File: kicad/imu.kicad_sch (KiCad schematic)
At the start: 3 parts, among them U7 BMI160

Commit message: checking shunt footprints
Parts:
- C36: renamed from C33; footprint (none) -> Capacitor_SMD:C_0402_1005Metric
- C37: renamed from C34; footprint (none) -> Capacitor_SMD:C_0402_1005Metric
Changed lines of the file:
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@@
 		(dnp no)
 		(fields_autoplaced yes)
-		(property "Reference" "#PWR043"
+		(property "Reference" "#PWR066"
 			(at 137.16 119.38 0)
 			(effects
@@
 			(project ""
 				(path "/83aea3b7-5b9b-498e-8d41-e84fae2f87fa/314ef610-7e67-4168-90f4-c11d9335fa4f"
-					(reference "#PWR043")
+					(reference "#PWR066")
 					(unit 1)
 				)
@@
 		(dnp no)
 		(fields_autoplaced yes)
-		(property "Reference" "C33"
+		(property "Reference" "C36"
 			(at 161.29 96.5199 0)
 			(effects
@@
 			)
 		)
-		(property "Footprint" ""
+		(property "Footprint" "Capacitor_SMD:C_0402_1005Metric"
 			(at 158.4452 101.6 0)
 			(effects
@@
 			(project ""
 				(path "/83aea3b7-5b9b-498e-8d41-e84fae2f87fa/314ef610-7e67-4168-90f4-c11d9335fa4f"
-					(reference "C33")
+					(reference "C36")
 					(unit 1)
 				)
@@
 		(dnp no)
 		(fields_autoplaced yes)
-		(property "Reference" "C34"
+		(property "Reference" "C37"
 			(at 173.99 96.5199 0)
 			(effects
@@
 			)
 		)
-		(property "Footprint" ""
+		(property "Footprint" "Capacitor_SMD:C_0402_1005Metric"
 			(at 171.1452 101.6 0)
 			(effects
@@
 			(project "resc"
 				(path "/83aea3b7-5b9b-498e-8d41-e84fae2f87fa/314ef610-7e67-4168-90f4-c11d9335fa4f"
-					(reference "C34")
+					(reference "C37")
 					(unit 1)
 				)
@@
 		(dnp no)
 		(fields_autoplaced yes)
-		(property "Reference" "#PWR042"
+		(property "Reference" "#PWR065"
 			(at 138.43 82.55 0)
 			(effects
@@
 			(project ""
 				(path "/83aea3b7-5b9b-498e-8d41-e84fae2f87fa/314ef610-7e67-4168-90f4-c11d9335fa4f"
-					(reference "#PWR042")
-					(unit 1)
-				)
+					(reference "#PWR065")
+					(unit 1)
+				)

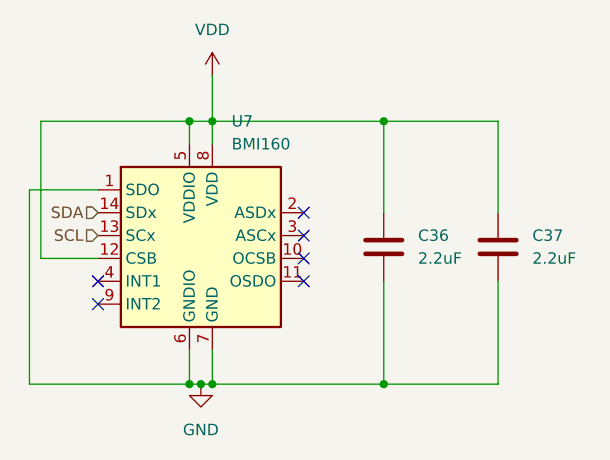
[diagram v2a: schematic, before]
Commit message: gate driver mostly schematic'd and pcb started
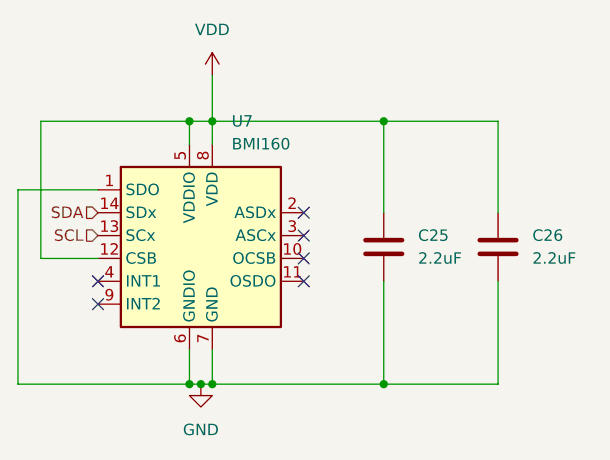
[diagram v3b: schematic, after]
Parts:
- renumbered C36 to C25, C37 to C26
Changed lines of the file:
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@@
 	(wire
 		(pts
-			(xy 118.11 113.03) (xy 135.89 113.03)
+			(xy 116.84 113.03) (xy 135.89 113.03)
 		)
 		(stroke
@@
 	(wire
 		(pts
-			(xy 125.73 91.44) (xy 118.11 91.44)
+			(xy 125.73 91.44) (xy 116.84 91.44)
 		)
 		(stroke
@@
 	(wire
 		(pts
-			(xy 118.11 91.44) (xy 118.11 113.03)
+			(xy 116.84 91.44) (xy 116.84 113.03)
 		)
 		(stroke
@@
 		(dnp no)
 		(fields_autoplaced yes)
-		(property "Reference" "#PWR066"
+		(property "Reference" "#PWR053"
 			(at 137.16 119.38 0)
 			(effects
@@
 			(project ""
 				(path "/83aea3b7-5b9b-498e-8d41-e84fae2f87fa/314ef610-7e67-4168-90f4-c11d9335fa4f"
-					(reference "#PWR066")
+					(reference "#PWR053")
 					(unit 1)
 				)
@@
 		(dnp no)
 		(fields_autoplaced yes)
-		(property "Reference" "C36"
+		(property "Reference" "C25"
 			(at 161.29 96.5199 0)
 			(effects
@@
 			(project ""
 				(path "/83aea3b7-5b9b-498e-8d41-e84fae2f87fa/314ef610-7e67-4168-90f4-c11d9335fa4f"
-					(reference "C36")
+					(reference "C25")
 					(unit 1)
 				)
@@
 		(dnp no)
 		(fields_autoplaced yes)
-		(property "Reference" "C37"
+		(property "Reference" "C26"
 			(at 173.99 96.5199 0)
 			(effects
@@
 			(project "resc"
 				(path "/83aea3b7-5b9b-498e-8d41-e84fae2f87fa/314ef610-7e67-4168-90f4-c11d9335fa4f"
-					(reference "C37")
+					(reference "C26")
 					(unit 1)
 				)
@@
 		(dnp no)
 		(fields_autoplaced yes)
-		(property "Reference" "#PWR065"
+		(property "Reference" "#PWR052"
 			(at 138.43 82.55 0)
 			(effects
@@
 			(project ""
 				(path "/83aea3b7-5b9b-498e-8d41-e84fae2f87fa/314ef610-7e67-4168-90f4-c11d9335fa4f"
-					(reference "#PWR065")
+					(reference "#PWR052")
 					(unit 1)
 				)

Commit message: rev3 ordered
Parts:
- renumbered C25 to C36, C26 to C37
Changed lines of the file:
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@@
 		(dnp no)
 		(fields_autoplaced yes)
-		(property "Reference" "#PWR053"
+		(property "Reference" "#PWR066"
 			(at 137.16 119.38 0)
 			(effects
@@
 			(project ""
 				(path "/83aea3b7-5b9b-498e-8d41-e84fae2f87fa/314ef610-7e67-4168-90f4-c11d9335fa4f"
-					(reference "#PWR053")
+					(reference "#PWR066")
 					(unit 1)
 				)
@@
 		(dnp no)
 		(fields_autoplaced yes)
-		(property "Reference" "C25"
+		(property "Reference" "C36"
 			(at 161.29 96.5199 0)
 			(effects
@@
 			(project ""
 				(path "/83aea3b7-5b9b-498e-8d41-e84fae2f87fa/314ef610-7e67-4168-90f4-c11d9335fa4f"
-					(reference "C25")
+					(reference "C36")
 					(unit 1)
 				)
@@
 		(dnp no)
 		(fields_autoplaced yes)
-		(property "Reference" "C26"
+		(property "Reference" "C37"
 			(at 173.99 96.5199 0)
 			(effects
@@
 			(project "resc"
 				(path "/83aea3b7-5b9b-498e-8d41-e84fae2f87fa/314ef610-7e67-4168-90f4-c11d9335fa4f"
-					(reference "C26")
+					(reference "C37")
 					(unit 1)
 				)
@@
 		(dnp no)
 		(fields_autoplaced yes)
-		(property "Reference" "#PWR052"
+		(property "Reference" "#PWR065"
 			(at 138.43 82.55 0)
 			(effects
@@
 			(project ""
 				(path "/83aea3b7-5b9b-498e-8d41-e84fae2f87fa/314ef610-7e67-4168-90f4-c11d9335fa4f"
-					(reference "#PWR052")
-					(unit 1)
-				)
+					(reference "#PWR065")
+					(unit 1)
+				)
